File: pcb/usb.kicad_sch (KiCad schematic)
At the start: 39 parts, among them J6 USB4105, J7 S2B-PH-SM4-TB, Q1 DMG3401LSN, Q2 DMG3418L, Q3 DMG3418L, SW1 LC2251EENP, U149 SN74LVC2G132DCUR, U151 AP2112K-3.3, U152 BQ297xy, U153 MCP73831-2-OT

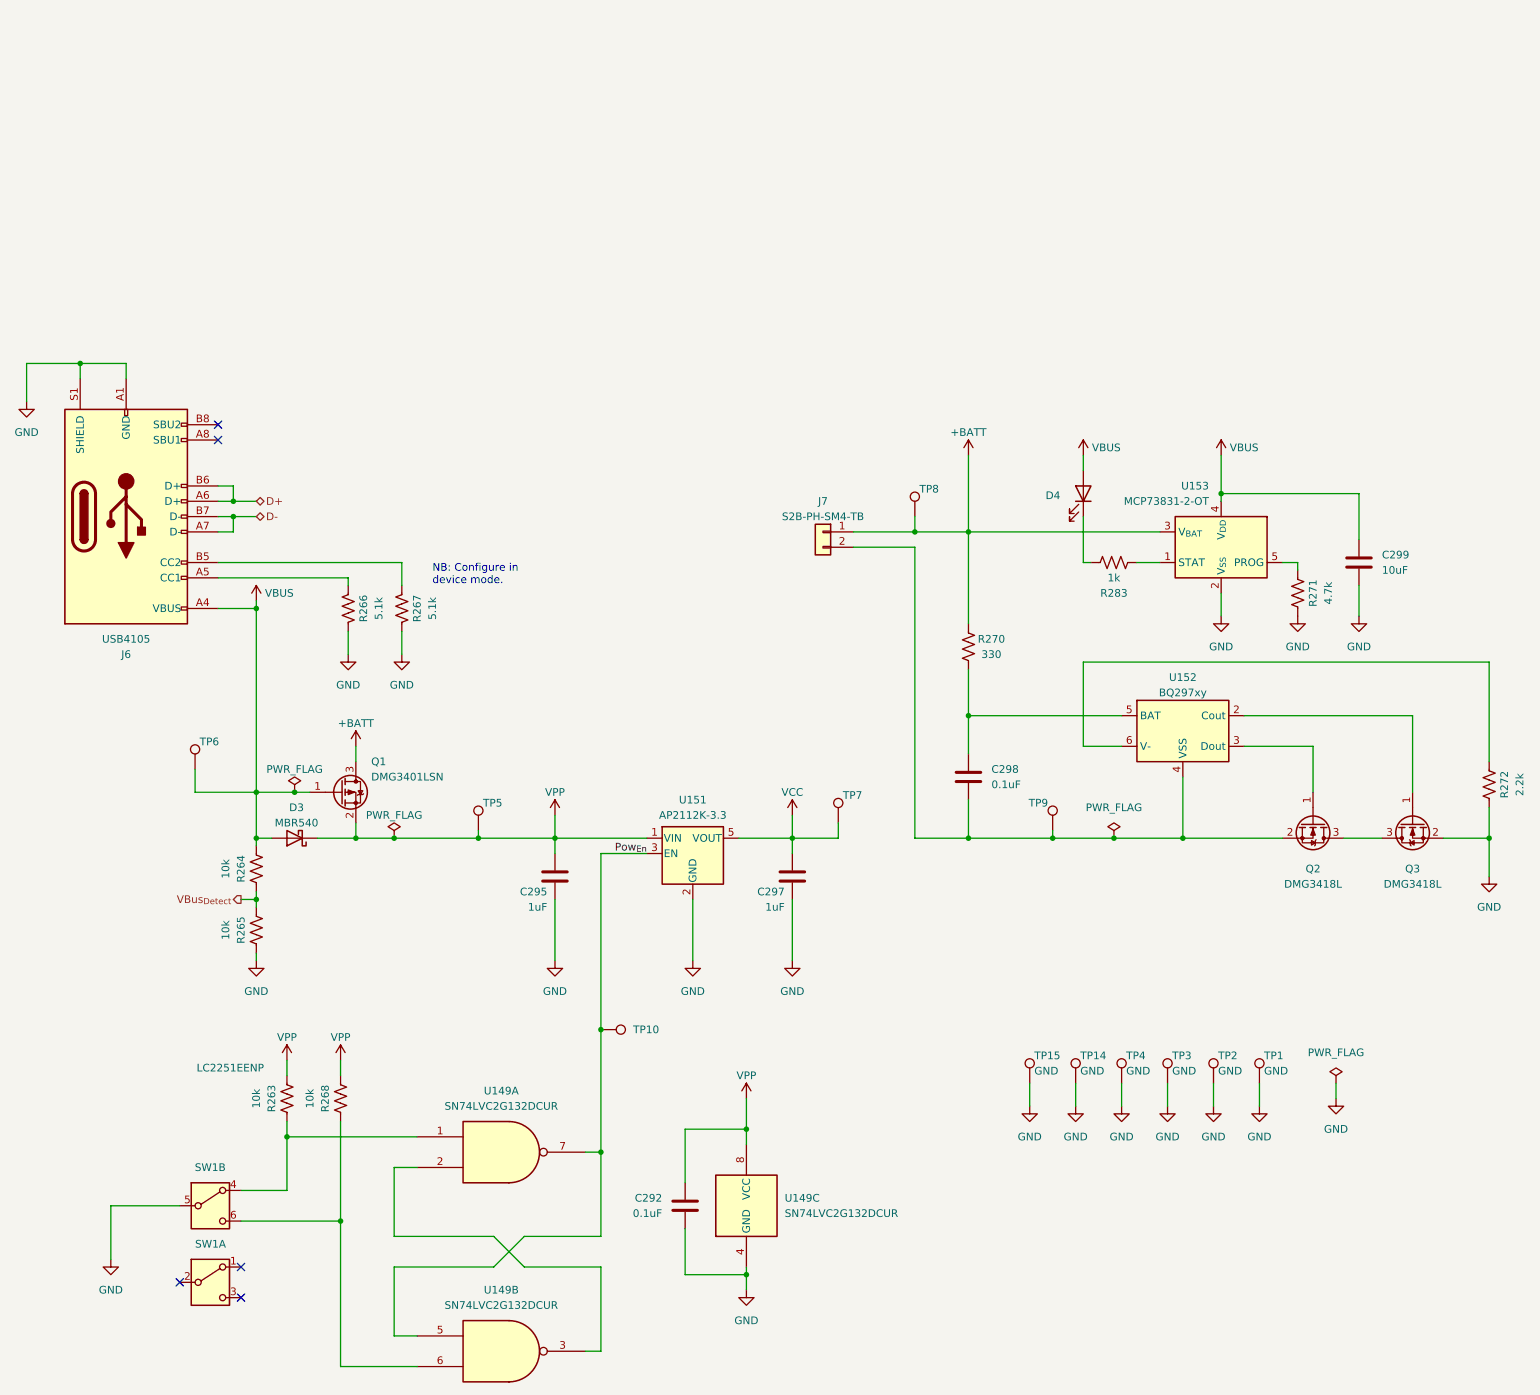
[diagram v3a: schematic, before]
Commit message: Fix MCP73831 subcircuit
- Add decoupling capacitor on Vbat
- Add more thermal support to layout (solid connection of ground to
  ground plane copper and addition of thermal vias)
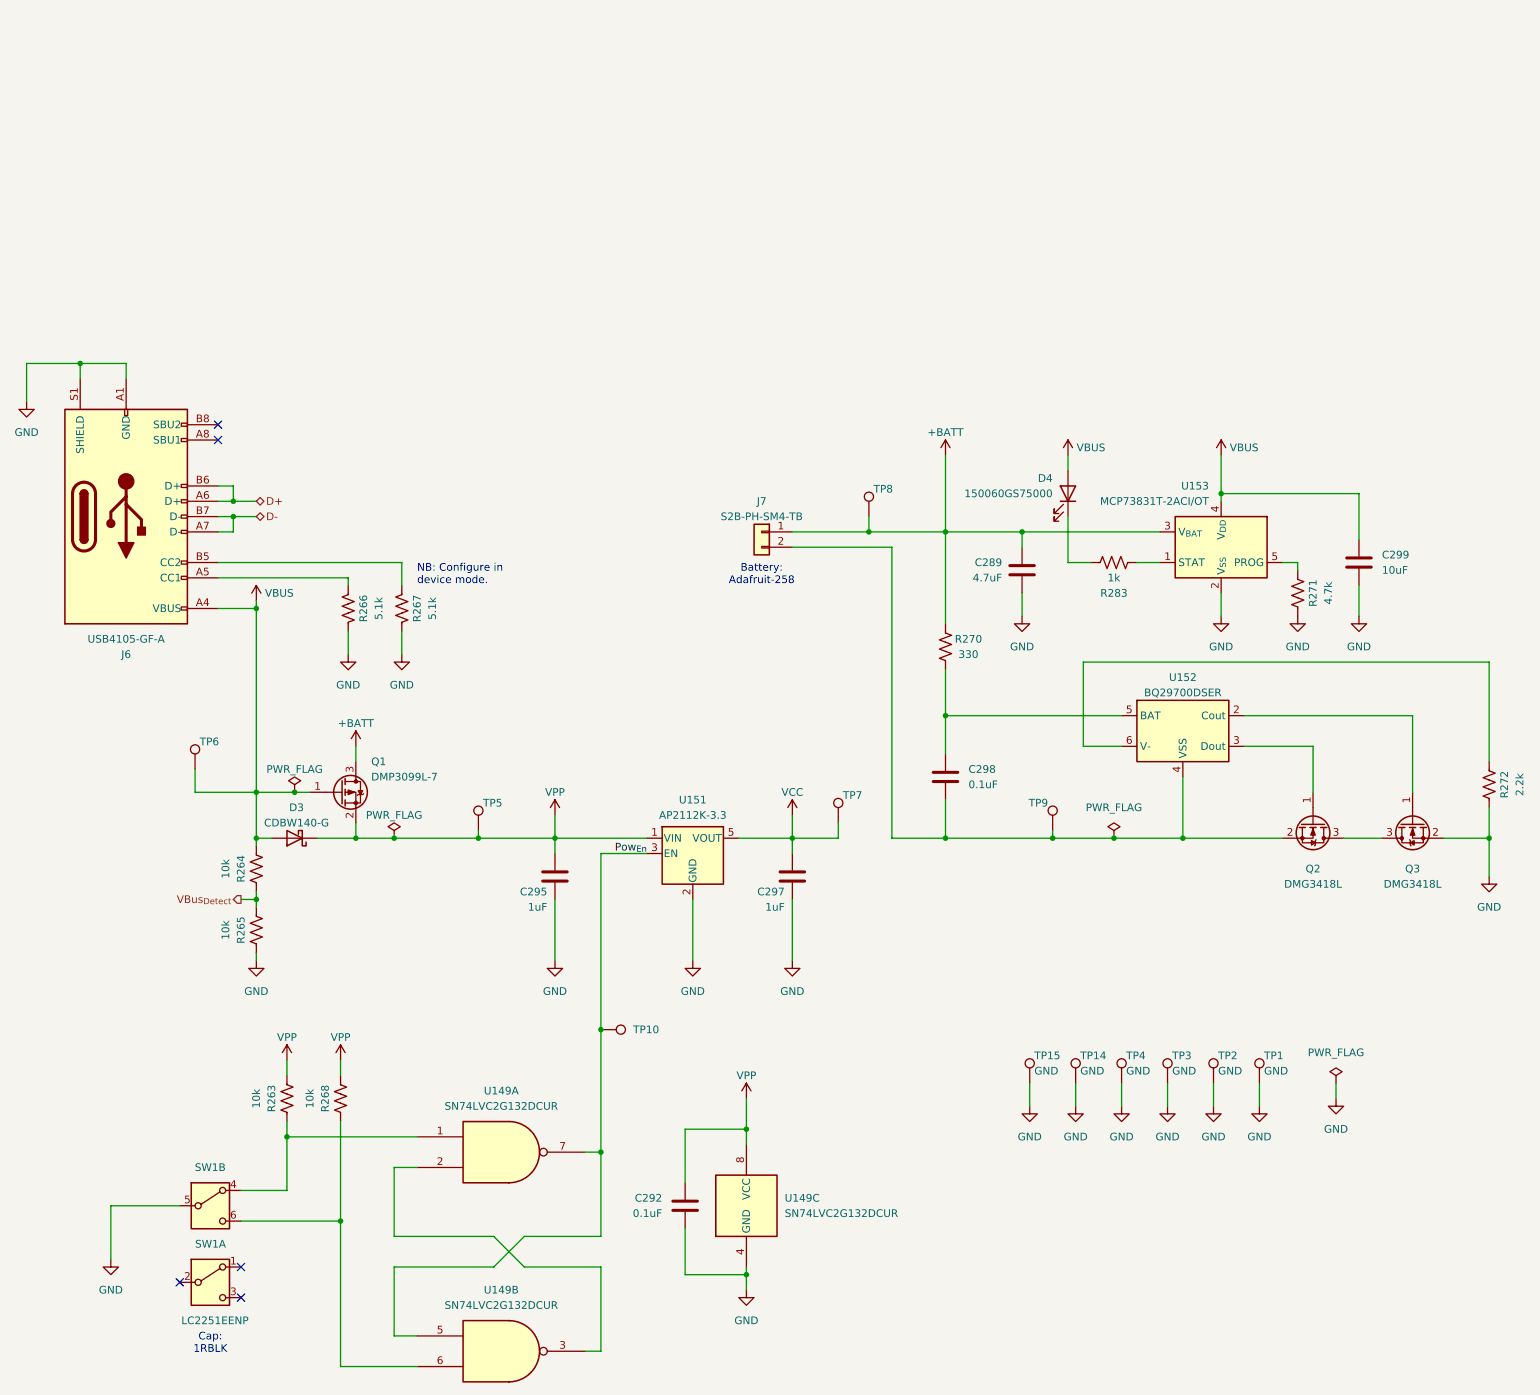
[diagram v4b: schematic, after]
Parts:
- added C289: 4.7uF, Capacitor_SMD:C_1206_3216Metric, symbol Device:C
- D3: value MBR540 -> CDBW140-G
- D4: value LED -> 150060GS75000
- J6: value USB4105 -> USB4105-GF-A
- Q1: value DMG3401LSN -> DMP3099L-7
- U152: value BQ297xy -> BQ29700DSER
- U153: value MCP73831-2-OT -> MCP73831T-2ACI/OT
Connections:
- net +BATT: now also C289.1
- net GND: now also C289.2
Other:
- note added: "Battery: Adafruit-258"
- note added: "Cap: 1RBLK"
- moved on the sheet: C298, D4, J7, R270, TP8

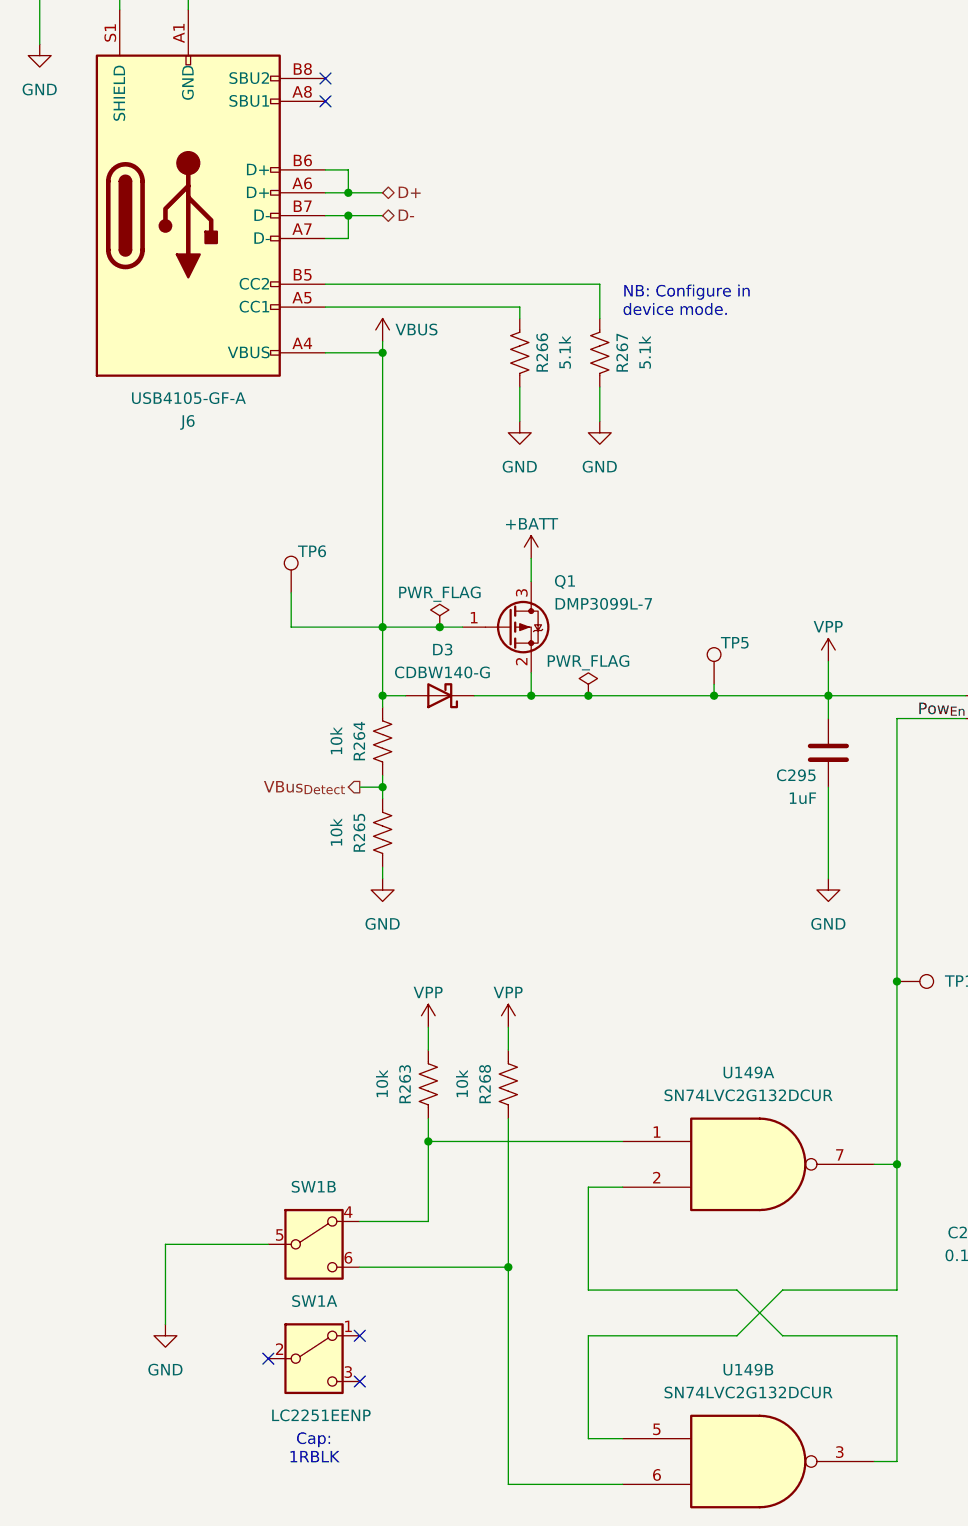
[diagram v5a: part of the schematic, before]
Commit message: Change power switch
- Replace push button with rocker
- Added some notches to outside of PCB for aligning with enclosure
- Upgrade to KiCAD 9.0
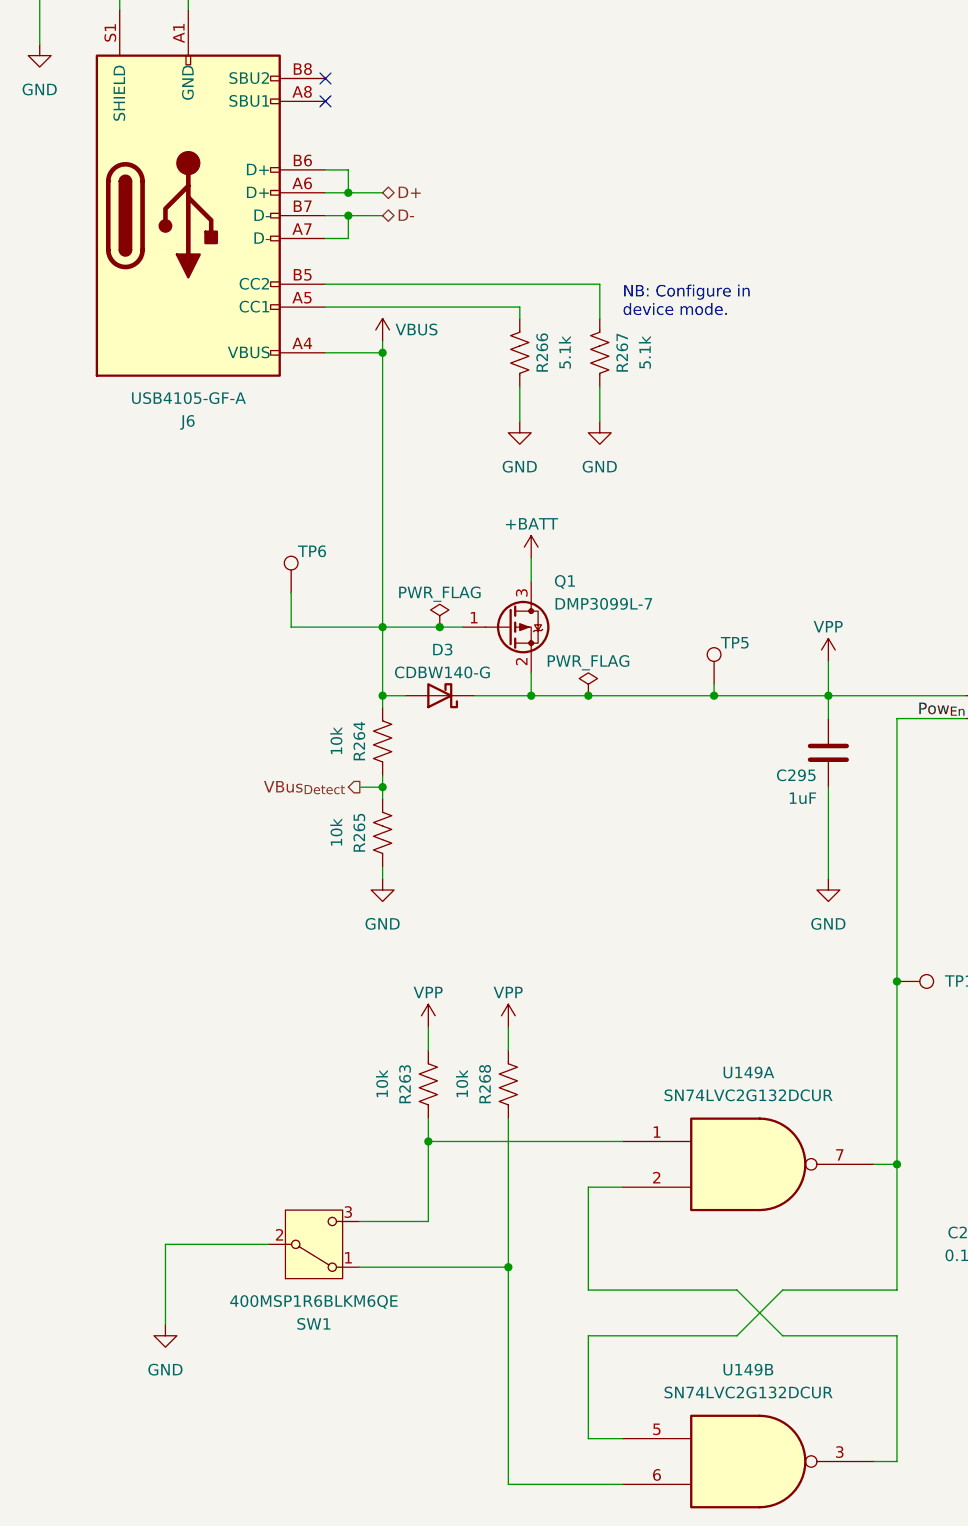
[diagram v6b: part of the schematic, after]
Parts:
- removed SW1: LC2251EENP, open-ephys:ESWITCH_LC2251EENP, symbol Switch:SW_DPDT_x2
- added SW1: 400MSP1R6BLKM6QE, open-ephys:ESWITCH_400MSPxR6xxxM6xE, symbol Switch:SW_SPDT
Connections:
- net GND: now also SW1.2 (B)
- net at R268.2, U149.6: now also SW1.1 (A)
- net at R263.2, U149.1: now also SW1.3 (C)
- no-connect marks 5 -> 2
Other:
- note removed: "Cap: 1RBLK"
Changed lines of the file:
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@@
 (kicad_sch
-	(version 20231120)
+	(version 20241209)
 	(generator "eeschema")
-	(generator_version "8.0")
+	(generator_version "9.0")
 	(paper "A4")
 	(title_block
@@
 		(comment 1 "Jonathan P. Newman")
 	)
+	(text "Battery:\nAdafruit-258\n"
+		(exclude_from_sim no)
+		(at 152.4 58.42 0)
+		(effects
+			(font
+				(size 1.27 1.27)
+			)
+			(justify bottom)
+		)
+	)
+	(text "NB: Configure in\ndevice mode."
+		(exclude_from_sim no)
+		(at 95.25 58.42 0)
+		(effects
+			(font
+				(size 1.27 1.27)
+			)
+			(justify left bottom)
+		)
+	)
 	(junction
 		(at 82.55 163.83)
@@
 	)
 	(no_connect
-		(at 66.04 176.53)
-	)
-	(no_connect
 		(at 62.23 34.29)
 	)
 	(no_connect
-		(at 66.04 171.45)
-	)
-	(no_connect
-		(at 55.88 173.99)
-	)
-	(no_connect
 		(at 62.23 31.75)
 	)
@@
 		)
 	)
-	(text "Battery:\nAdafruit-258\n"
-		(exclude_from_sim no)
-		(at 152.4 58.42 0)
-		(effects
-			(font
-				(size 1.27 1.27)
-			)
-			(justify bottom)
-		)
-	)
-	(text "NB: Configure in\ndevice mode."
-		(exclude_from_sim no)
-		(at 95.25 58.42 0)
-		(effects
-			(font
-				(size 1.27 1.27)
-			)
-			(justify left bottom)
-		)
-	)
-	(text "Cap:\n1RBLK"
-		(exclude_from_sim no)
-		(at 60.96 184.15 0)
-		(effects
-			(font
-				(size 1.27 1.27)
-			)
-		)
-	)
 	(label "Pow_{En}"
 		(at 133.35 102.87 180)
-		(fields_autoplaced yes)
 		(effects
 			(font
@@
 		(shape output)
 		(at 66.04 110.49 180)
-		(fields_autoplaced yes)
 		(effects
 			(font
@@
 		(shape bidirectional)
 		(at 68.58 46.99 0)
-		(fields_autoplaced yes)
 		(effects
 			(font
@@
 		(shape bidirectional)
 		(at 68.58 44.45 0)
-		(fields_autoplaced yes)
 		(effects
 			(font
@@
 	)
 	(symbol
-		(lib_id "Switch:SW_DPDT_x2")
-		(at 60.96 173.99 0)
-		(unit 1)
-		(exclude_from_sim no)
-		(in_bom yes)
-		(on_board yes)
-		(dnp no)
-		(property "Reference" "SW1"
-			(at 58.42 167.64 0)
-			(effects
-				(font
-					(size 1.27 1.27)
-				)
-				(justify left)
-			)
-		)
-		(property "Value" "LC2251EENP"
-			(at 58.42 170.18 90)
-			(effects
-				(font
-					(size 1.27 1.27)
-				)
-				(justify left)
-				(hide yes)
-			)
-		)
-		(property "Footprint" "open-ephys:ESWITCH_LC2251EENP"
-			(at 60.96 173.99 0)
-			(effects
-				(font
-					(size 1.27 1.27)
-				)
-				(hide yes)
-			)
-		)
-		(property "Datasheet" "https://www.digikey.com/htmldatasheets/production/45702/0/0/1/lc2251eenp-drawing.pdf"
-			(at 60.96 173.99 0)
-			(effects
-				(font
-					(size 1.27 1.27)
-				)
-				(hide yes)
-			)
-		)
-		(property "Description" "Switch, dual pole double throw, separate symbols"
-			(at 60.96 173.99 0)
-			(effects
-				(font
-					(size 1.27 1.27)
-				)
-				(hide yes)
-			)
-		)
-		(property "Voltage" ""
-			(at 60.96 173.99 0)
-			(effects
-				(font
-					(size 1.27 1.27)
-				)
-				(hide yes)
-			)
-		)
-		(property "Datasheet1" ""
-			(at 60.96 173.99 0)
-			(effects
-				(font
-					(size 1.27 1.27)
-				)
-				(hide yes)
-			)
-		)
-		(property "Part No." ""
-			(at 60.96 173.99 0)
-			(effects
-				(font
-					(size 1.27 1.27)
-				)
-				(hide yes)
-			)
-		)
-		(pin "1"
-		)
-		(pin "2"
-		)
-		(pin "3"
-		)
-		(pin "4"
-		)
-		(pin "5"
-		)
-		(pin "6"
-		)
-		(instances
-			(project "ephys-test-board"
-				(path "/ffaa6ffd-73fa-4da3-9ff1-78fa7369281f/3204537c-edba-465e-8dbf-7f75aa43b711"
-					(reference "SW1")
-					(unit 1)
-				)
-			)
-		)
-	)
-	(symbol
 		(lib_id "Device:R_US")
 		(at 68.58 115.57 0)
@@
 	)
 	(symbol
-		(lib_id "Switch:SW_DPDT_x2")
-		(at 60.96 161.29 0)
-		(unit 2)
-		(exclude_from_sim no)
-		(in_bom yes)
-		(on_board yes)
-		(dnp no)
-		(property "Reference" "SW1"
-			(at 63.5 154.94 0)
-			(effects
-				(font
-					(size 1.27 1.27)
-				)
-				(justify right)
-			)
-		)
-		(property "Value" "LC2251EENP"
-			(at 67.31 180.34 0)
-			(effects
-				(font
-					(size 1.27 1.27)
-				)
-				(justify right)
-			)
-		)
-		(property "Footprint" "open-ephys:ESWITCH_LC2251EENP"
-			(at 60.96 161.29 0)
-			(effects
-				(font
-					(size 1.27 1.27)
-				)
-				(hide yes)
-			)
-		)
-		(property "Datasheet" "https://www.digikey.com/htmldatasheets/production/45702/0/0/1/lc2251eenp-drawing.pdf"
-			(at 60.96 161.29 0)
-			(effects
-				(font
-					(size 1.27 1.27)
-				)
-				(hide yes)
-			)
-		)
-		(property "Description" "Switch, dual pole double throw, separate symbols"
-			(at 60.96 161.29 0)
-			(effects
-				(font
-					(size 1.27 1.27)
-				)
-				(hide yes)
-			)
-		)
-		(property "Voltage" ""
-			(at 60.96 161.29 0)
-			(effects
-				(font
-					(size 1.27 1.27)
-				)
-				(hide yes)
-			)
-		)
-		(property "Datasheet1" ""
-			(at 60.96 161.29 0)
-			(effects
-				(font
-					(size 1.27 1.27)
-				)
-				(hide yes)
-			)
-		)
-		(property "Part No." ""
-			(at 60.96 161.29 0)
-			(effects
-				(font
-					(size 1.27 1.27)
-				)
-				(hide yes)
-			)
-		)
-		(pin "1"
-		)
-		(pin "2"
-		)
-		(pin "3"
-		)
-		(pin "4"
-		)
-		(pin "5"
-		)
-		(pin "6"
-		)
-		(instances
-			(project "ephys-test-board"
-				(path "/ffaa6ffd-73fa-4da3-9ff1-78fa7369281f/3204537c-edba-465e-8dbf-7f75aa43b711"
-					(reference "SW1")
-					(unit 2)
-				)
-			)
-		)
-	)
-	(symbol
 		(lib_id "power:GND")
 		(at 273.05 106.68 0)
@@
 					(unit 1)
 				)
+			)
+		)
+	)
+	(symbol
+		(lib_id "Switch:SW_SPDT")
+		(at 60.96 161.29 0)
+		(mirror x)
+		(unit 1)
+		(exclude_from_sim no)
+		(in_bom yes)
+		(on_board yes)
+		(dnp no)
+		(property "Reference" "SW1"
+			(at 60.96 170.18 0)
+			(effects
+				(font
+					(size 1.27 1.27)
+				)
+			)
+		)
+		(property "Value" "400MSP1R6BLKM6QE"
+			(at 60.96 167.64 0)
+			(effects
+				(font
+					(size 1.27 1.27)
+				)
+			)
+		)
+		(property "Footprint" "open-ephys:ESWITCH_400MSPxR6xxxM6xE"
+			(at 60.96 161.29 0)
+			(effects
+				(font
+					(size 1.27 1.27)
+				)
+				(hide yes)
+			)
+		)
+		(property "Datasheet" "~"
+			(at 60.96 153.67 0)
+			(effects
+				(font
+					(size 1.27 1.27)
+				)
+				(hide yes)
+			)
+		)
+		(property "Description" "Switch, single pole double throw"
+			(at 60.96 161.29 0)
+			(effects
+				(font
+					(size 1.27 1.27)
+				)
+				(hide yes)
+			)
+		)
+		(pin "1"
+		)
+		(pin "2"
+		)
+		(pin "3"
+		)
+		(instances
+			(project "ephys-test-board"
+				(path "/ffaa6ffd-73fa-4da3-9ff1-78fa7369281f/3204537c-edba-465e-8dbf-7f75aa43b711"
+					(reference "SW1")
+					(unit 1)
+				)
